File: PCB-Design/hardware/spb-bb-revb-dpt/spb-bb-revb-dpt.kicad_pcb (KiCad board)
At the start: 4 copper layers, 89.5 x 85.2 mm, 226 parts, among them J1 DC+, J10 U.FL H2, J11 U.FL L2, J12 V_ISO,HS in: 1 +, 2 -, J13 V_ISO,LS in: 1 +, 2 -, J14 CTRL2: 1 RTN 2 PWMH 3 RTN 4 P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, J15 MMCX VDS L3, J16 U.FL H3, J17 U.FL L3, J18 MMCX VDS L4, J19 U.FL H4, J2 DC-, J20 U.FL L4, J21 AC, J3 V_ISO,HS in: 1 +, 2 -, J4 V_ISO,LS in: 1 +, 2 -, J5 CTRL1: 1 RTN 2 PWMH 3 RTN 4 P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, J6 MMCX VDS L1, J7 U.FL H1, J8 U.FL L1, J9 MMCX VDS L2, Q1 EPC2361, Q2 EPC2361, Q3 EPC2361, Q4 EPC2361, Q5 EPC2361, Q6 EPC2361, Q7 EPC2361, Q8 EPC2361, U1 2EDF7275K, U2 2EDF7275K

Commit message: DPT board: every test point carries its name on the silk
- Test-point labels are placed with the point, within 1.6 mm of the
  (signal) pad (last round 3 mm), full name or without the block digit.
  A point without room for its label is moved; if none fits it is not
  placed and fab/testpoints.csv names an existing pad to probe instead
  (DIS1, VDDI2, DIS2 on the dense driver input side).
- Control-side test points stay on the top: bottom ones need vias that
  split the narrow GNDI pour.
- Pour-split blame now uses everything a test point added (pads, stubs,
  vias); fallback vias respect via keepouts.
32 test points, all labelled; DRC 0/0 (also fresh load of the saved
project), schematic = PCB, no 3D collisions.

Co-Authored-By: Claude Opus 5.5 <noreply@anthropic.com>
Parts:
- removed TP21: VDDI2, spb_fab:TestPoint_Pad_D1.0mm
- removed TP24: DIS2, spb_fab:TestPoint_Pad_D1.0mm
- removed TP6: DIS1, spb_fab:TestPoint_Pad_D1.0mm
- moved TP45 8.35 mm to (138.2, 81.0)
- moved TP1 6.99 mm to (121.0, 126.5)
- moved TP19 6.99 mm to (168.6, 126.5)
- moved TP3 0.20 mm to (127.8, 123.7)
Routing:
- net DCP: track 2.75 -> 6.36 mm
- net VDDI2: track 5.95 -> 4.80 mm
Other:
- board text added: "+12V2"
- board text added: "GNDI1"
- board text added: "VDDI1"

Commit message: DPT board: fabrication review fixes - gate re-layout, mirrored DC- vias, fab package
- G1/G2: R_G at the gate pad, Kelvin return beside the gate on L1 to the corridor,
  Kelvin rows joined under the star (HS L4, LS L2), point-symmetric about each star
  (the two cells of a row are rotated 180 deg); 10k pull-downs as 0402 between the rows
- G3: 0R U.FL gate-sense links DNP by default
- P1: shunt-return via rows counted from the inner edge, all DC- vias mirrored
- F1/F2: fab notes in the Gerber zip (stack-up, rules, tenting, via-in-pad list),
  separate PTH/NPTH drill files
- F4: BOM grouped by value, RS1-RS4 lab-fitted (not in pick-and-place)
- loop_post: cell-to-cell loop mutual matrix; gate model refs follow the new R_G
- generator QUICK=1 mode (DRC after fill, no test points)
- review document with the dispositions

DRC 0/0 (also fresh load), sch = PCB, no 3D collisions, 36 labelled test points.

Co-Authored-By: Claude Opus 5.5 <noreply@anthropic.com>
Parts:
- added TP18: VGS Q4, spb_fab:TestPoint_Spring_1.0_GND1.5-6.0, B.Cu at (132.8, 108.0)
- added TP36: VGS Q8, spb_fab:TestPoint_Spring_1.0_GND1.5-6.0, B.Cu at (180.2, 108.0)
- added TP37: VDS Q3, spb_fab:TestPoint_Spring_1.0_GND1.5-6.0, B.Cu at (118.8, 112.0)
- added TP41: VDS Q7, spb_fab:TestPoint_Spring_1.0_GND1.5-6.0, B.Cu at (166.2, 112.0)
- R16, R18, R35, R37: value 0R (V_GS HS) -> DNP 0R (V_GS HS, fit to use the U.FL)
- R17, R19, R36, R38: value 0R (V_GS LS) -> DNP 0R (V_GS LS, fit to use the U.FL)
- R22, R3: value 0R5 1% (R_G LL) -> 10k 1% (HS gate pull-down); footprint Resistor_SMD:R_0603_1608Metric -> Resistor_SMD:R_0402_1005Metric
- R23, R4: value 0R5 1% (R_G LR) -> 0R5 1% (R_G LL)
- R24, R5: value 10k 1% (HS gate pull-down) -> 0R5 1% (R_G LR)
- R25, R6: footprint Resistor_SMD:R_0603_1608Metric -> Resistor_SMD:R_0402_1005Metric
- moved R23 8.61 mm to (168.2, 109.5), turned to 90 degrees
- moved R4 8.61 mm to (120.7, 109.5), turned to 90 degrees
- moved R24 6.01 mm to (179.3, 108.9)
- moved R5 6.01 mm to (131.8, 108.9)
- moved R22 4.95 mm to (170.8, 104.2), turned to 90 degrees
- moved R3 4.95 mm to (123.2, 104.2), turned to 90 degrees
- moved R25 3.76 mm to (170.8, 108.5)
- moved R6 3.76 mm to (123.2, 108.5)
- moved TP17 3.22 mm to (121.2, 108.8)
- moved TP35 3.22 mm to (168.7, 108.8)
- moved R2 2.62 mm to (131.8, 104.6), turned to 90 degrees
- moved R21 2.62 mm to (179.3, 104.6), turned to 90 degrees
- moved R1 2.62 mm to (120.7, 105.2), turned to 90 degrees
- moved R20 2.62 mm to (168.2, 105.2), turned to 90 degrees
- moved TP16 1.02 mm to (132.2, 103.9)
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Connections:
- R22 pad 1: GL_L2 -> GH_STAR2
- R22 pad 2: GL_STAR2 -> KH2
- R23 pad 1: GL_STAR2 -> GL_L2
- R23 pad 2: GL_R2 -> GL_STAR2
- R24 pad 1: KH2 -> GL_STAR2
- R24 pad 2: GH_STAR2 -> GL_R2
- R3 pad 1: GL_L1 -> GH_STAR1
- R3 pad 2: GL_STAR1 -> KH1
- R4 pad 1: GL_STAR1 -> GL_L1
- R4 pad 2: GL_R1 -> GL_STAR1
- R5 pad 1: KH1 -> GL_STAR1
- R5 pad 2: GH_STAR1 -> GL_R1
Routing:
- net GL_STAR1: track 10.3 -> 17.1 mm
- net GL_STAR2: track 10.3 -> 17.1 mm
- net GH_STAR1: track 14.1 -> 20.9 mm
- net GH_STAR2: track 14.1 -> 20.9 mm
- net KH2: track 101.6 -> 106.5 mm, vias 5 -> 6
- net KH1: track 101.6 -> 106.5 mm, vias 5 -> 6
- net GH_R2: track 7.82 -> 4.08 mm
- net GH_R1: track 7.82 -> 4.08 mm
- net GL_R2: track 7.32 -> 3.59 mm
- net GL_R1: track 7.32 -> 3.59 mm
- net GH_L2: track 7.32 -> 3.59 mm
- net GH_L1: track 7.32 -> 3.59 mm
- net GL_L2: track 8.89 -> 5.64 mm
- net GL_L1: track 8.89 -> 5.64 mm
- net KL2: track 106.5 -> 109.1 mm, vias 7 -> 6
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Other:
- board text added: "VDS Q3"
- board text added: "VDS Q7"
- board text added: "VGS Q4"
- board text added: "VGS Q8"

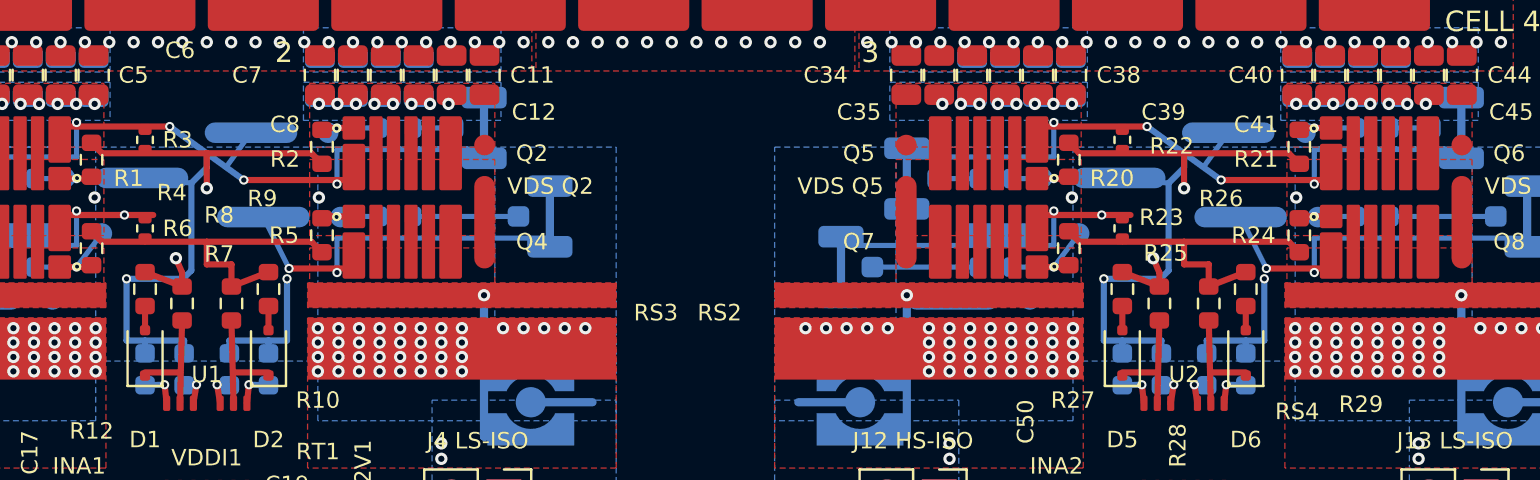
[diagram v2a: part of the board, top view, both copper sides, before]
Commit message: DPT board: gate loops paired with their Kelvin returns to the driver caps
Q3D showed the shared star -> driver part dominating the gate loop. Rounds 2/3:
- HS Kelvin rows join on L2 (0.1 mm under the L1 star) instead of L4
- Kelvin returns follow the gate path on the adjacent layer all the way to the
  1 uF output caps (HS: L2 / L4 / L2 under L1 / L3 / L1, LS: L2 under L1),
  island supply vias (x = +-3.9) are side branches without gate current
- test points: only a test point that is itself open is dropped after the fill
  (the rule dropped the V_GS Q4/Q8 spring pads next to a V_DS pad)

Gate loop HS 15.4 -> 12.5 nH, LS 9.7 -> 7.6 nH (single FET), pair-driven 25.4 -> 20.6 /
16.6 -> 12.3 nH; gate-power coupling <= 8.5 pH. SPICE HS V_DS peak 106.3 -> 100.3 V at
R_G,on 2 Ohm, 94.0 V at 2.5 Ohm. DRC 0/0 (fresh load too), sch = PCB, no 3D collisions,
36 labelled test points (all eight V_GS spring pads).

Co-Authored-By: Claude Opus 5.5 <noreply@anthropic.com>
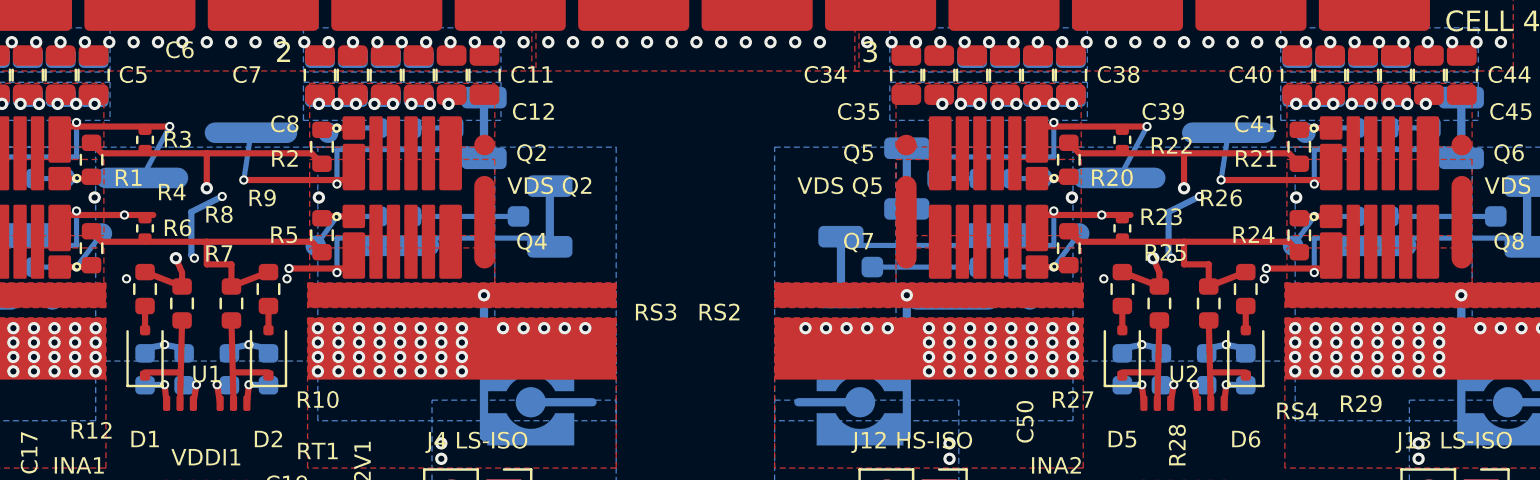
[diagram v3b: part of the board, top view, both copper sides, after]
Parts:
- moved TP18 1.84 mm to (131.6, 109.4), turned to 0 degrees
- moved TP36 1.84 mm to (179.1, 109.4), turned to 0 degrees
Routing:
- net KL1: track 109.1 -> 105.7 mm, vias 6 -> 7
- net KL2: track 109.1 -> 105.7 mm, vias 6 -> 7
- net GL_R2: track 3.59 -> 5.36 mm
- net GL_R1: track 3.59 -> 5.36 mm
- net KH2: track 106.5 -> 107.2 mm, vias 6 -> 9
- net KH1: track 106.5 -> 107.2 mm, vias 6 -> 9

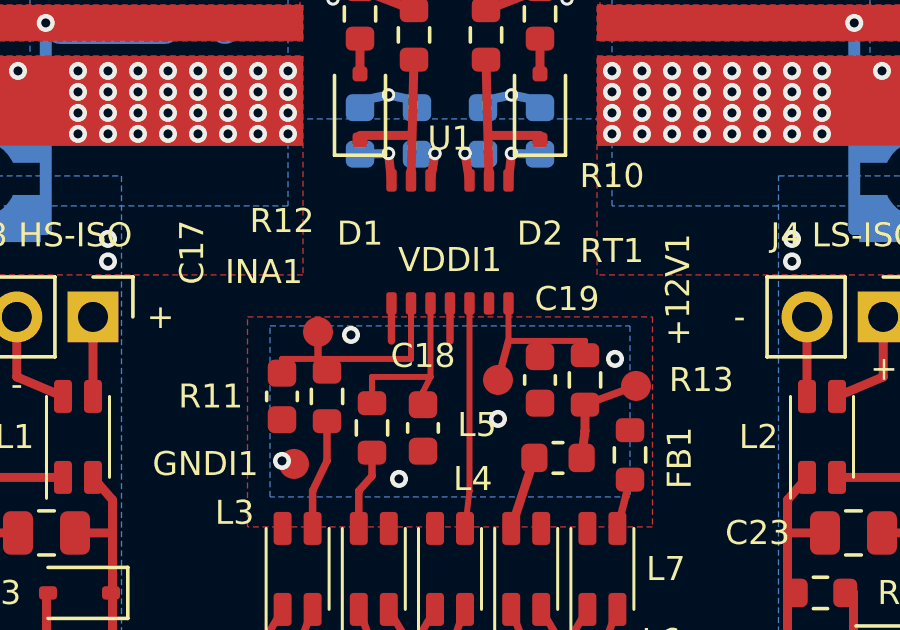
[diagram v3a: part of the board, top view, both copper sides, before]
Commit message: DPT board: R_ON 1.0 Ohm (R_G,on 2.5 Ohm per device)
- R7/R9/R26/R28 0.75 -> 1.0 Ohm (Yageo RC0603FR-071RL): with the extracted gate
  network the HS V_DS peak at the LS turn-on drops from 100.0 V to 93.7 V (75 V, 322 A),
  E_on 105 uJ (= design-flow value), cell spread E_on 0.2 %, I_off +-2.2 % (inner vs outer
  cells, power side)
- SPICE: sweep varies R_ON with R_G fixed at 0.5 Ohm (R_G = R_G,on - 2 R_ON went to 0);
  block 2 is block 1 shifted, not mirrored (cell 3 <-> 1, 4 <-> 2); the 1.25 Ohm case
  diverged numerically and is dropped
- DRC 0/0 (fresh load too), sch = PCB, no 3D collisions, 36 test points

Co-Authored-By: Claude Opus 5.5 <noreply@anthropic.com>
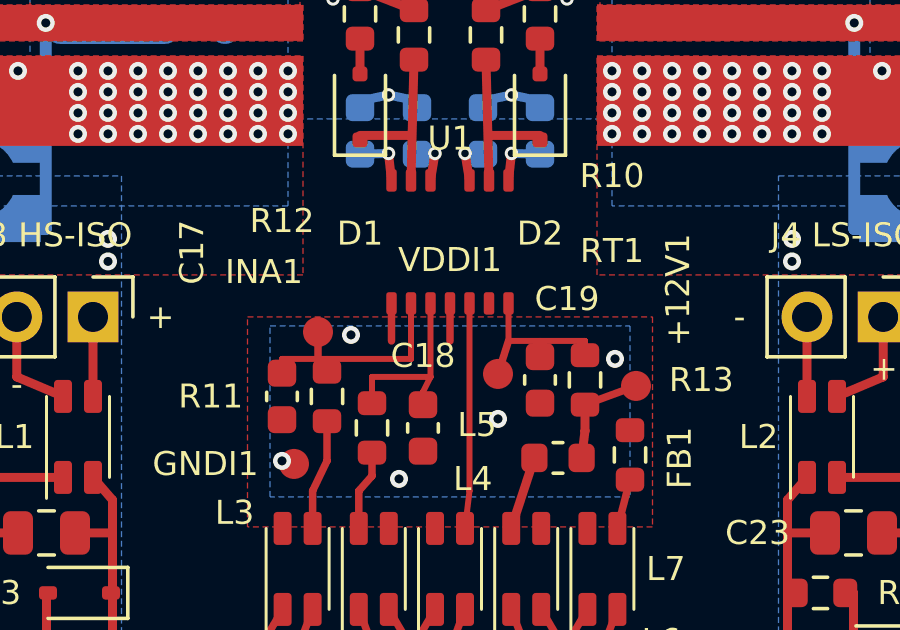
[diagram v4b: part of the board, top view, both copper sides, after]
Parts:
- R26, R7: value 0R75 1% (R_ON,A) -> 1R0 1% (R_ON,A)
- R28, R9: value 0R75 1% (R_ON,B) -> 1R0 1% (R_ON,B)
- moved TP3 0.20 mm to (127.8, 123.5)

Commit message: DPT board: R_ON 1.5 Ohm and -1.9 V gate off-bias; SPICE shunt inductance fixed
- SPICE: the UFCS shunt's 120 pH was written as Lser on a resistor, which LTspice
  rejects and ignores; now a separate inductor. Part body ESLs added to the gate
  network (0603 R_G / R_ON / R_OFF 0.4 nH, D_OFF 1 nH); gate off level -1.9 V
  (V_ISO 7 V with the 5.1 V Zener); the lumped-gate case had been commented out
- with the corrected model R_ON 1.0 Ohm gives a 105 V HS V_DS peak: R_ON 1.5 Ohm
  (R7/R9/R26/R28, Yageo RC0603FR-071R5L, R_G,on 3.5 Ohm) gives 92.9 V, E_on 125 uJ,
  E_off 20 uJ; V_GS bump on the held-off FET -0.50 ... -0.76 V (was +1.4 V at 0 V off)
- DPT_measurement_setup: gate-drive settings (V_ISO 7 V, R_ON, one PWM source and
  equal cables for U1/U2); review document 10.2
- DRC 0/0 (fresh load too), sch = PCB, no 3D collisions, 36 test points

Co-Authored-By: Claude Opus 5.5 <noreply@anthropic.com>
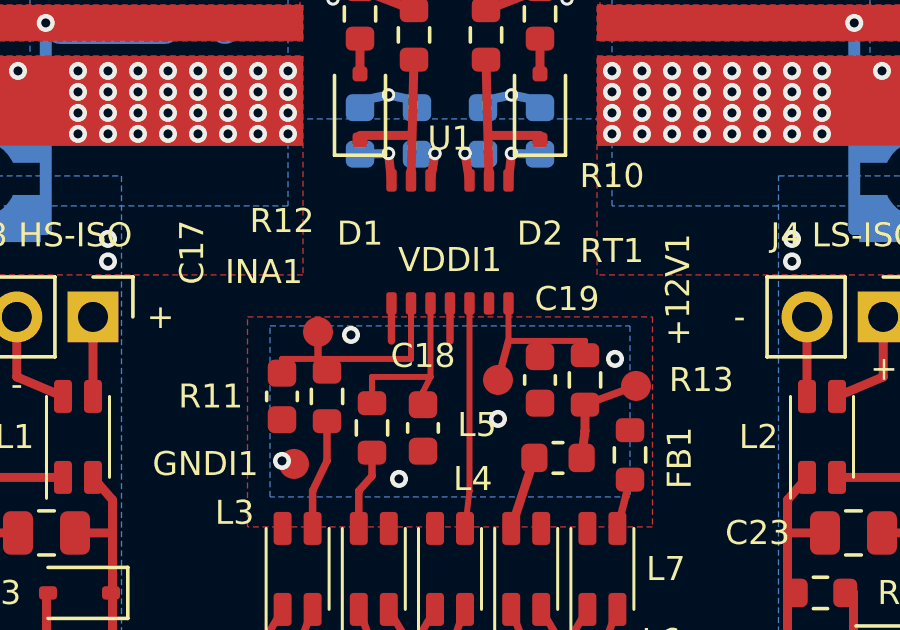
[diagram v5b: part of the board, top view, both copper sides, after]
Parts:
- R26, R7: value 1R0 1% (R_ON,A) -> 1R5 1% (R_ON,A)
- R28, R9: value 1R0 1% (R_ON,B) -> 1R5 1% (R_ON,B)
- moved TP3 0.20 mm to (127.8, 123.7)
